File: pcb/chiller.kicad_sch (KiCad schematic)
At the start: 39 parts, among them J1 Conn_01x03, J10 Current Sense, J11 Conn_01x14, J12 Debug, J2 Conn_01x03, J3 Ext, J4 Conn_01x02, J5 Conn_01x02, J6 Conn_01x02, J7 Conn_01x02, J8 Conn_01x02, J9 CONN_01X02, K1 G5LE-1, K2 G6B-1114C-US5DC, Q1 MMBT3904, Q2 MMBT3904, Q3 BSS138, Q4 BSS138, U1 ESP32-WROOM-32, U2 DSN-MINI-360, U3 AP1117-33

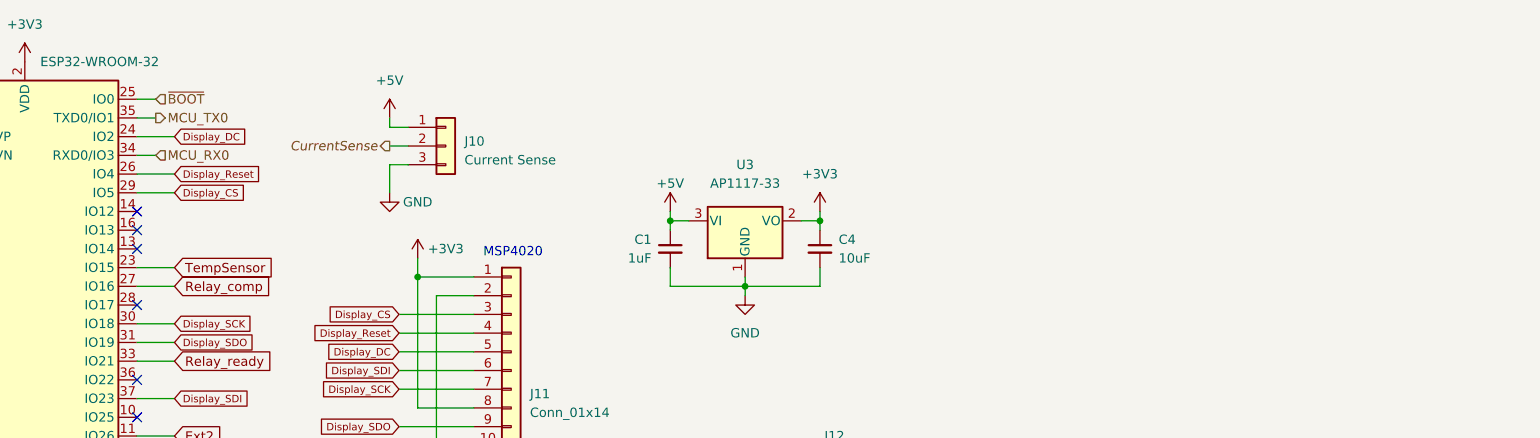
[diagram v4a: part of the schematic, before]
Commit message: Finish routing.
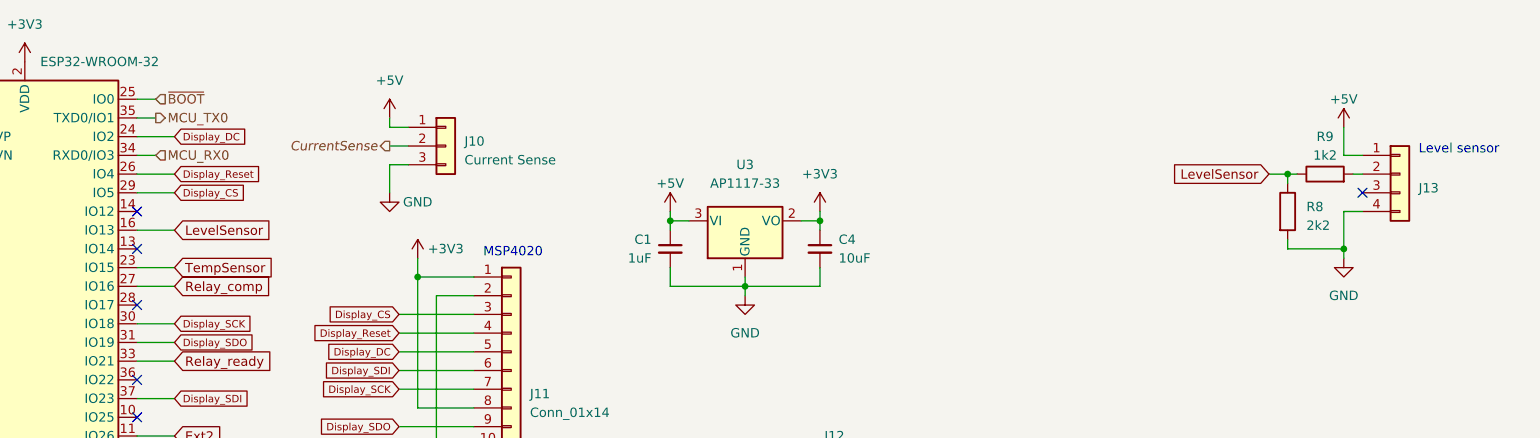
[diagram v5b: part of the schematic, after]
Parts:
- added J13: Conn_01x04, Connector_JST:JST_XH_B4B-XH-A_1x04_P2.50mm_Vertical, symbol Connector_Generic:Conn_01x04
- added R8: 2k2, Resistor_SMD:R_0603_1608Metric, symbol Device:R
- added R9: 1k2, Resistor_SMD:R_0603_1608Metric, symbol Device:R
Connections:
- net +5V: now also J13.1 (Pin_1)
- net GND: now also J13.4 (Pin_4), R8.2
- net LevelSensor: now reaches U1.16 (IO13)
- net LevelSensor: now also R8.1, R9.1
- new net: J13.2 (Pin_2), R9.2
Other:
- note added: "Level sensor"
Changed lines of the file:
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@@
   (junction (at 176.53 203.2) (diameter 1.016) (color 0 0 0 0)
   )
+  (junction (at 245.11 39.37) (diameter 0) (color 0 0 0 0)
+  )
   (junction (at 121.92 175.26) (diameter 0) (color 0 0 0 0)
   )
@@
   )
   (junction (at 163.83 175.26) (diameter 0) (color 0 0 0 0)
+  )
+  (junction (at 252.73 49.53) (diameter 0) (color 0 0 0 0)
   )
   (junction (at 163.83 149.86) (diameter 0) (color 0 0 0 0)
@@
   (no_connect (at 138.43 132.08))
   (no_connect (at 88.9 67.31))
-  (no_connect (at 88.9 46.99))
   (no_connect (at 134.62 76.2))
   (no_connect (at 134.62 81.28))
@@
   (no_connect (at 88.9 57.15))
   (no_connect (at 88.9 80.01))
+  (no_connect (at 255.27 41.91))
   (no_connect (at 134.62 86.36))
   (no_connect (at 88.9 44.45))
@@
     (stroke (width 0) (type default))
   )
+  (wire (pts (xy 254 39.37) (xy 255.27 39.37))
+    (stroke (width 0) (type default))
+  )
   (wire (pts (xy 35.56 83.82) (xy 35.56 85.09))
     (stroke (width 0) (type default))
@@
     (stroke (width 0) (type default))
   )
+  (wire (pts (xy 245.11 39.37) (xy 245.11 40.64))
+    (stroke (width 0) (type default))
+  )
   (wire (pts (xy 88.9 39.37) (xy 93.98 39.37))
     (stroke (width 0) (type default))
@@
   )
   (wire (pts (xy 124.46 60.96) (xy 134.62 60.96))
+    (stroke (width 0) (type default))
+  )
+  (wire (pts (xy 252.73 44.45) (xy 255.27 44.45))
     (stroke (width 0) (type default))
   )
@@
     (stroke (width 0) (type solid))
   )
+  (wire (pts (xy 252.73 49.53) (xy 252.73 50.8))
+    (stroke (width 0) (type default))
+  )
+  (wire (pts (xy 252.73 36.83) (xy 255.27 36.83))
+    (stroke (width 0) (type default))
+  )
   (wire (pts (xy 125.73 215.9) (xy 125.73 223.52))
     (stroke (width 0) (type solid))
@@
     (stroke (width 0) (type default))
   )
+  (wire (pts (xy 88.9 46.99) (xy 93.98 46.99))
+    (stroke (width 0) (type default))
+  )
   (wire (pts (xy 57.15 137.16) (xy 64.77 137.16))
     (stroke (width 0) (type default))
   )
   (wire (pts (xy 181.61 44.45) (xy 181.61 45.72))
+    (stroke (width 0) (type default))
+  )
+  (wire (pts (xy 242.57 39.37) (xy 245.11 39.37))
     (stroke (width 0) (type default))
   )
@@
     (stroke (width 0) (type default))
   )
+  (wire (pts (xy 245.11 48.26) (xy 245.11 49.53))
+    (stroke (width 0) (type default))
+  )
   (wire (pts (xy 33.02 83.82) (xy 35.56 86.36))
     (stroke (width 0) (type default))
@@
     (stroke (width 0) (type default))
   )
+  (wire (pts (xy 252.73 44.45) (xy 252.73 49.53))
+    (stroke (width 0) (type default))
+  )
+  (wire (pts (xy 245.11 49.53) (xy 252.73 49.53))
+    (stroke (width 0) (type default))
+  )
   (wire (pts (xy 24.13 78.74) (xy 27.94 78.74))
     (stroke (width 0) (type default))
@@
   )
   (wire (pts (xy 63.5 121.92) (xy 64.77 121.92))
+    (stroke (width 0) (type default))
+  )
+  (wire (pts (xy 252.73 33.02) (xy 252.73 36.83))
     (stroke (width 0) (type default))
   )
@@
   )
   (wire (pts (xy 33.02 87.63) (xy 24.13 87.63))
+    (stroke (width 0) (type default))
+  )
+  (wire (pts (xy 245.11 39.37) (xy 246.38 39.37))
     (stroke (width 0) (type default))
   )
@@
   (text "Temp sensor 2" (exclude_from_sim no)
  (at 81.28 135.89 0)
+    (effects (font (size 1.27 1.27)) (justify left bottom))
+  )
+  (text "Level sensor" (exclude_from_sim no)
+ (at 262.89 36.83 0)
     (effects (font (size 1.27 1.27)) (justify left bottom))
   )
@@
     )
   )
+  (global_label "LevelSensor" (shape input) (at 93.98 46.99 0) (fields_autoplaced)
+    (effects (font (size 1.27 1.27)) (justify left))
+    (property "Intersheetrefs" "${INTERSHEET_REFS}" (at 108.1343 46.99 0)
+      (effects (font (size 1.27 1.27)) (justify left) hide)
+    )
+  )
   (global_label "Display_Reset" (shape input) (at 124.46 60.96 180) (fields_autoplaced)
     (effects (font (size 1 1)) (justify right))
@@
     (property "Intersheetrefs" "${INTERSHEET_REFS}" (at 114.4648 58.3575 0)
       (effects (font (size 1 1)) (justify right) hide)
+    )
+  )
+  (global_label "LevelSensor" (shape input) (at 242.57 39.37 180) (fields_autoplaced)
+    (effects (font (size 1.27 1.27)) (justify right))
+    (property "Intersheetrefs" "${INTERSHEET_REFS}" (at 228.4157 39.37 0)
+      (effects (font (size 1.27 1.27)) (justify right) hide)
     )
   )
@@
     )
   )
+  (symbol (lib_id "power:GND") (at 252.73 50.8 0) (unit 1)
+    (in_bom yes) (on_board yes) (dnp no) (fields_autoplaced)
+    (property "Reference" "#PWR028" (at 252.73 57.15 0)
+      (effects (font (size 1.27 1.27)) hide)
+    )
+    (property "Value" "GND" (at 252.73 55.88 0)
+      (effects (font (size 1.27 1.27)))
+    )
+    (property "Footprint" "" (at 252.73 50.8 0)
+      (effects (font (size 1.27 1.27)) hide)
+    )
+    (property "Datasheet" "" (at 252.73 50.8 0)
+      (effects (font (size 1.27 1.27)) hide)
+    )
+    (pin "1")
+    (instances
+      (project "chiller"
+        (path "/212a0d71-cc7b-49f8-b4ca-a935e5355dca"
+          (reference "#PWR028") (unit 1)
+        )
+      )
+    )
+  )
   (symbol (lib_id "Device:R") (at 173.99 168.91 0) (unit 1)
     (in_bom yes) (on_board yes) (dnp no) (fields_autoplaced)
@@
         (path "/212a0d71-cc7b-49f8-b4ca-a935e5355dca"
           (reference "J12") (unit 1)
+        )
+      )
+    )
+  )
+  (symbol (lib_id "Connector_Generic:Conn_01x04") (at 260.35 39.37 0) (unit 1)
+    (in_bom yes) (on_board yes) (dnp no) (fields_autoplaced)
+    (property "Reference" "J13" (at 262.89 41.275 0)
+      (effects (font (size 1.27 1.27)) (justify left))
+    )
+    (property "Value" "Conn_01x04" (at 262.89 42.545 0)
+      (effects (font (size 1.27 1.27)) (justify left) hide)
+    )
+    (property "Footprint" "Connector_JST:JST_XH_B4B-XH-A_1x04_P2.50mm_Vertical" (at 260.35 39.37 0)
+      (effects (font (size 1.27 1.27)) hide)
+    )
+    (property "Datasheet" "~" (at 260.35 39.37 0)
+      (effects (font (size 1.27 1.27)) hide)
+    )
+    (pin "1")
+    (pin "2")
+    (pin "3")
+    (pin "4")
+    (instances
+      (project "chiller"
+        (path "/212a0d71-cc7b-49f8-b4ca-a935e5355dca"
+          (reference "J13") (unit 1)
         )
       )
@@
     )
   )
+  (symbol (lib_id "power:+5V") (at 252.73 33.02 0) (unit 1)
+    (in_bom yes) (on_board yes) (dnp no) (fields_autoplaced)
+    (property "Reference" "#PWR027" (at 252.73 36.83 0)
+      (effects (font (size 1.27 1.27)) hide)
+    )
+    (property "Value" "+5V" (at 252.73 29.21 0)
+      (effects (font (size 1.27 1.27)))
+    )
+    (property "Footprint" "" (at 252.73 33.02 0)
+      (effects (font (size 1.27 1.27)) hide)
+    )
+    (property "Datasheet" "" (at 252.73 33.02 0)
+      (effects (font (size 1.27 1.27)) hide)
+    )
+    (pin "1")
+    (instances
+      (project "chiller"
+        (path "/212a0d71-cc7b-49f8-b4ca-a935e5355dca"
+          (reference "#PWR027") (unit 1)
+        )
+      )
+    )
+  )
+  (symbol (lib_id "Device:R") (at 250.19 39.37 90) (unit 1)
+    (in_bom yes) (on_board yes) (dnp no) (fields_autoplaced)
+    (property "Reference" "R9" (at 250.19 34.29 90)
+      (effects (font (size 1.27 1.27)))
+    )
+    (property "Value" "1k2" (at 250.19 36.83 90)
+      (effects (font (size 1.27 1.27)))
+    )
+    (property "Footprint" "Resistor_SMD:R_0603_1608Metric" (at 250.19 41.148 90)
+      (effects (font (size 1.27 1.27)) hide)
+    )
+    (property "Datasheet" "~" (at 250.19 39.37 0)
+      (effects (font (size 1.27 1.27)) hide)
+    )
+    (pin "1")
+    (pin "2")
+    (instances
+      (project "chiller"
+        (path "/212a0d71-cc7b-49f8-b4ca-a935e5355dca"
+          (reference "R9") (unit 1)
+        )
+      )
+    )
+  )
   (symbol (lib_id "Device:R_Small") (at 165.1 92.71 0) (mirror y) (unit 1)
     (in_bom yes) (on_board yes) (dnp no)
@@
         )
       )
+    )
+  )
+  (symbol (lib_id "Device:R") (at 245.11 44.45 0) (unit 1)
+    (in_bom yes) (on_board yes) (dnp no) (fields_autoplaced)
+    (property "Reference" "R8" (at 247.65 43.815 0)
+      (effects (font (size 1.27 1.27)) (justify left))
+    )
+    (property "Value" "2k2" (at 247.65 46.355 0)
+      (effects (font (size 1.27 1.27)) (justify left))
+    )
+    (property "Footprint" "Resistor_SMD:R_0603_1608Metric" (at 243.332 44.45 90)
+      (effects (font (size 1.27 1.27)) hide)
+    )
+    (property "Datasheet" "~" (at 245.11 44.45 0)
+      (effects (font (size 1.27 1.27)) hide)
+    )
+    (pin "1")
+    (pin "2")
+    (instances
+      (project "chiller"
+        (path "/212a0d71-cc7b-49f8-b4ca-a935e5355dca"
+          (reference "R8") (unit 1)
+        )
+      )

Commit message: Cleanup.
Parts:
- C1: value 1uF -> 1u
- C4: value 10uF -> 10u
- C5: value C -> 100n
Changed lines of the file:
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@@
   (symbol (lib_id "Device:C_Small") (at 181.61 49.53 0) (unit 1)
     (in_bom yes) (on_board yes) (dnp no) (fields_autoplaced)
-    (property "Reference" "C4" (at 184.15 48.2599 0)
-      (effects (font (size 1.27 1.27)) (justify left))
-    )
-    (property "Value" "10uF" (at 184.15 50.7999 0)
+    (property "Reference" "C4" (at 184.15 48.9013 0)
+      (effects (font (size 1.27 1.27)) (justify left))
+    )
+    (property "Value" "10u" (at 184.15 51.4413 0)
       (effects (font (size 1.27 1.27)) (justify left))
     )
@@
       (effects (font (size 1.27 1.27)) (justify left))
     )
-    (property "Value" "C" (at 36.83 41.275 0)
+    (property "Value" "100n" (at 36.83 41.275 0)
       (effects (font (size 1.27 1.27)) (justify left))
     )
@@
       (effects (font (size 1.27 1.27)) (justify left))
     )
-    (property "Value" "1uF" (at 158.75 50.7999 0)
-      (effects (font (size 1.27 1.27)) (justify left))
-    )
+    (property "Value" "1u" (at 158.75 50.7999 0)
+      (effects (font (size 1.27 1.27)) (justify left))
+    )

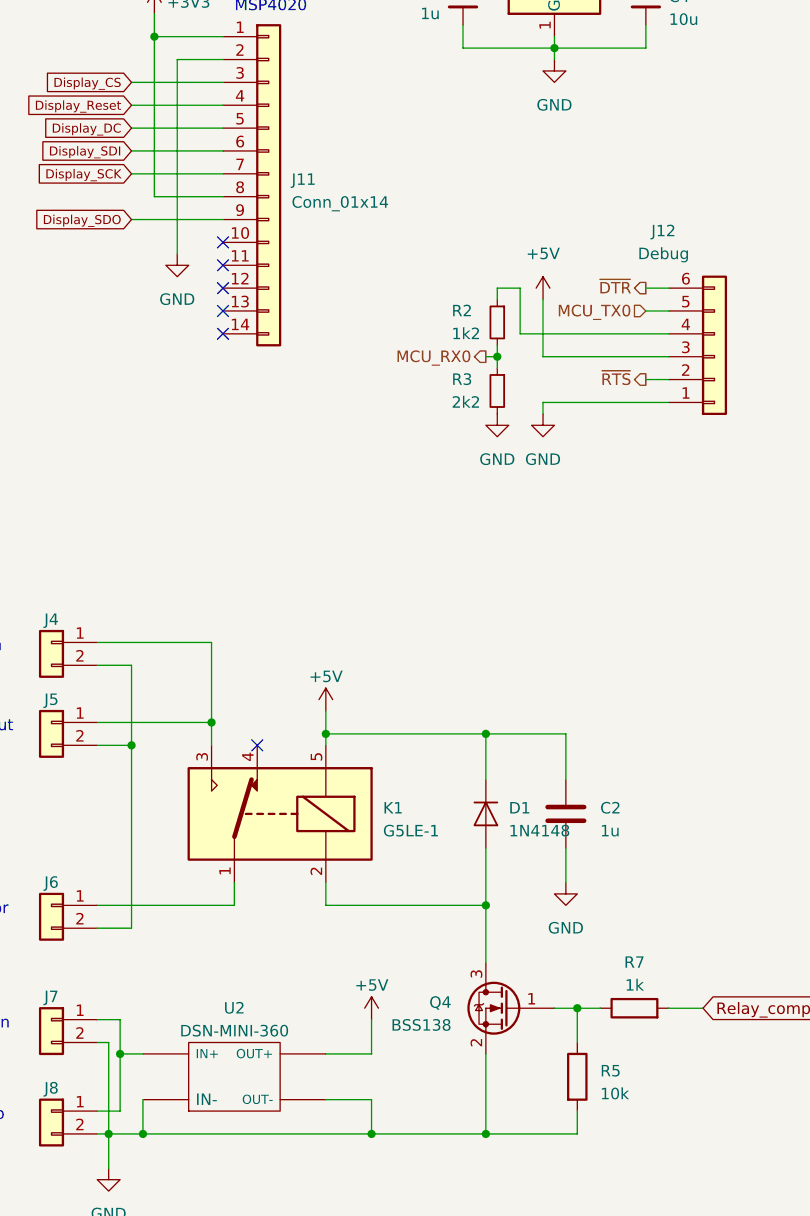
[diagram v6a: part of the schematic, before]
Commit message: Add diodes.
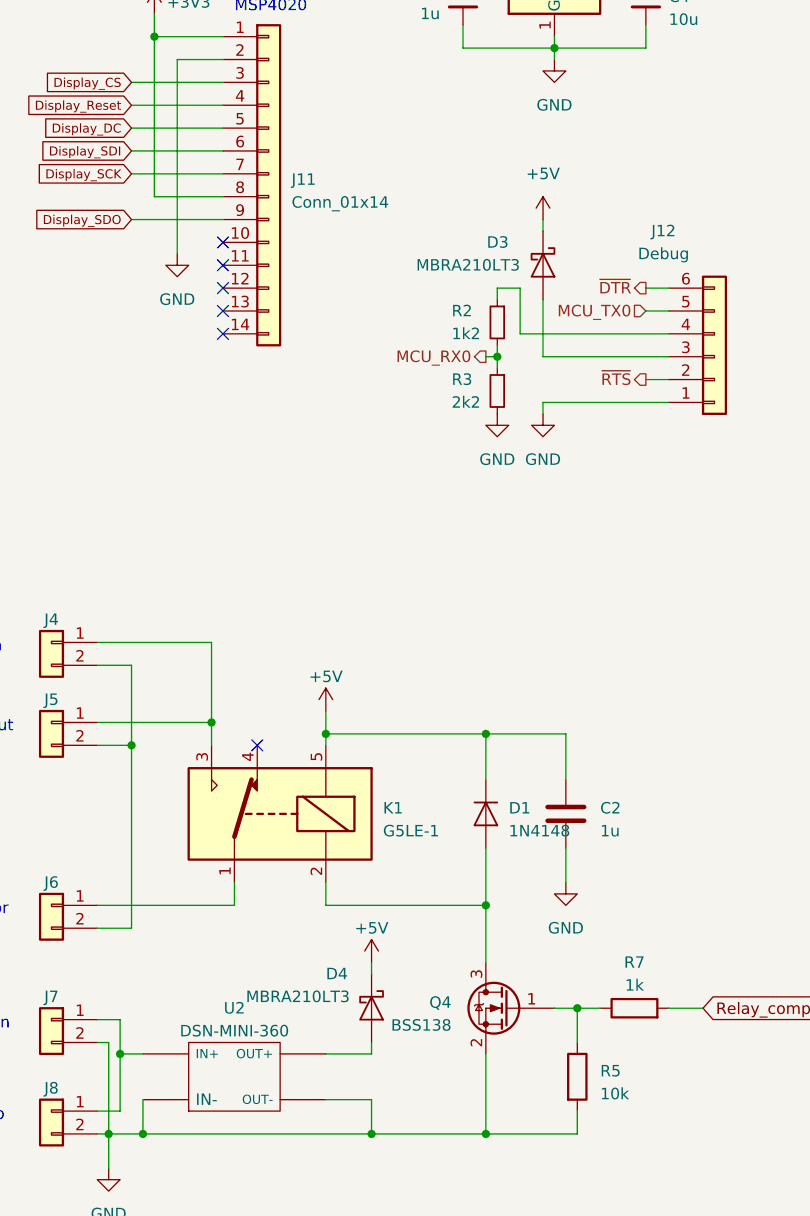
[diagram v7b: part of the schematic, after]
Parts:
- added D3, D4: MBRA210LT3, Diode_SMD:D_SMA, symbol Device:D_Schottky
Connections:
- net +5V: now also D3.1 (K), D4.1 (K); no longer J12.3 (Pin_3), U2.OUT+
- new net: D3.2 (A), J12.3 (Pin_3)
- new net: D4.2 (A), U2.OUT+
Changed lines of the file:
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@@
+    (stroke (width 0) (type default))
+  )
+  (wire (pts (xy 151.13 165.1) (xy 151.13 166.37))
     (stroke (width 0) (type default))
   )
@@
     (stroke (width 0) (type default))
   )
-  (wire (pts (xy 151.13 162.56) (xy 151.13 166.37))
-    (stroke (width 0) (type default))
-  )
   (wire (pts (xy 120.65 165.1) (xy 121.92 165.1))
     (stroke (width 0) (type default))
@@
     (stroke (width 0) (type default))
   )
+  (wire (pts (xy 170.18 73.66) (xy 170.18 74.93))
+    (stroke (width 0) (type default))
+  )
   (wire (pts (xy 165.1 87.63) (xy 165.1 88.9))
     (stroke (width 0) (type default))
@@
   )
   (wire (pts (xy 242.57 39.37) (xy 245.11 39.37))
+    (stroke (width 0) (type default))
+  )
+  (wire (pts (xy 151.13 156.21) (xy 151.13 157.48))
     (stroke (width 0) (type default))
   )
@@
     )
   )
-  (symbol (lib_id "power:+5V") (at 151.13 162.56 0) (unit 1)
-    (in_bom yes) (on_board yes) (dnp no) (fields_autoplaced)
-    (property "Reference" "#PWR014" (at 151.13 166.37 0)
-      (effects (font (size 1.27 1.27)) hide)
-    )
-    (property "Value" "+5V" (at 151.13 158.75 0)
-      (effects (font (size 1.27 1.27)))
-    )
-    (property "Footprint" "" (at 151.13 162.56 0)
-      (effects (font (size 1.27 1.27)) hide)
-    )
-    (property "Datasheet" "" (at 151.13 162.56 0)
+  (symbol (lib_id "Device:D_Schottky") (at 170.18 78.74 270) (unit 1)
+    (in_bom yes) (on_board yes) (dnp no)
+    (property "Reference" "D3" (at 166.37 76.2 90)
+      (effects (font (size 1.27 1.27)) (justify right))
+    )
+    (property "Value" "MBRA210LT3 " (at 167.64 78.74 90)
+      (effects (font (size 1.27 1.27)) (justify right))
+    )
+    (property "Footprint" "Diode_SMD:D_SMA" (at 170.18 78.74 0)
+      (effects (font (size 1.27 1.27)) hide)
+    )
+    (property "Datasheet" "~" (at 170.18 78.74 0)
+      (effects (font (size 1.27 1.27)) hide)
+    )
+    (pin "1")
+    (pin "2")
+    (instances
+      (project "chiller"
+        (path "/212a0d71-cc7b-49f8-b4ca-a935e5355dca"
+          (reference "D3") (unit 1)
+        )
+      )
+    )
+  )
+  (symbol (lib_id "power:+5V") (at 151.13 156.21 0) (unit 1)
+    (in_bom yes) (on_board yes) (dnp no) (fields_autoplaced)
+    (property "Reference" "#PWR014" (at 151.13 160.02 0)
+      (effects (font (size 1.27 1.27)) hide)
+    )
+    (property "Value" "+5V" (at 151.13 152.4 0)
+      (effects (font (size 1.27 1.27)))
+    )
+    (property "Footprint" "" (at 151.13 156.21 0)
+      (effects (font (size 1.27 1.27)) hide)
+    )
+    (property "Datasheet" "" (at 151.13 156.21 0)
       (effects (font (size 1.27 1.27)) hide)
     )
@@
     )
   )
-  (symbol (lib_id "power:+5V") (at 170.18 82.55 0) (unit 1)
-    (in_bom yes) (on_board yes) (dnp no) (fields_autoplaced)
-    (property "Reference" "#PWR018" (at 170.18 86.36 0)
-      (effects (font (size 1.27 1.27)) hide)
-    )
-    (property "Value" "+5V" (at 170.18 77.47 0)
-      (effects (font (size 1.27 1.27)))
-    )
-    (property "Footprint" "" (at 170.18 82.55 0)
-      (effects (font (size 1.27 1.27)) hide)
-    )
-    (property "Datasheet" "" (at 170.18 82.55 0)
+  (symbol (lib_id "power:+5V") (at 170.18 73.66 0) (unit 1)
+    (in_bom yes) (on_board yes) (dnp no) (fields_autoplaced)
+    (property "Reference" "#PWR018" (at 170.18 77.47 0)
+      (effects (font (size 1.27 1.27)) hide)
+    )
+    (property "Value" "+5V" (at 170.18 68.58 0)
+      (effects (font (size 1.27 1.27)))
+    )
+    (property "Footprint" "" (at 170.18 73.66 0)
+      (effects (font (size 1.27 1.27)) hide)
+    )
+    (property "Datasheet" "" (at 170.18 73.66 0)
       (effects (font (size 1.27 1.27)) hide)
     )
@@
         )
       )
+    )
+  )
+  (symbol (lib_id "Device:D_Schottky") (at 151.13 161.29 270) (unit 1)
+    (in_bom yes) (on_board yes) (dnp no)
+    (property "Reference" "D4" (at 146.05 157.48 90)
+      (effects (font (size 1.27 1.27)) (justify left))
+    )
+    (property "Value" "MBRA210LT3 " (at 137.16 160.02 90)
+      (effects (font (size 1.27 1.27)) (justify left))
+    )
+    (property "Footprint" "Diode_SMD:D_SMA" (at 151.13 161.29 0)
+      (effects (font (size 1.27 1.27)) hide)
+    )
+    (property "Datasheet" "~" (at 151.13 161.29 0)
+      (effects (font (size 1.27 1.27)) hide)
+    )
+    (pin "1")
+    (pin "2")
+    (instances
+      (project "chiller"
+        (path "/212a0d71-cc7b-49f8-b4ca-a935e5355dca"
+          (reference "D4") (unit 1)
+        )
+      )

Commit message: Start adding forgotten features.
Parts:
- added J14: Flow sensor, Connector_JST:JST_XH_B3B-XH-A_1x03_P2.50mm_Vertical, symbol Connector_Generic:Conn_01x03
- added J15: Fan, Connector_JST:JST_XH_B2B-XH-A_1x02_P2.50mm_Vertical, symbol Connector_Generic:Conn_01x02
- added Q5: BSS138, Package_TO_SOT_SMD:SOT-23, symbol Device:Q_NMOS_GSD
- added R10: 1k2, Resistor_SMD:R_0603_1608Metric, symbol Device:R
- added R11: 2k2, Resistor_SMD:R_0603_1608Metric, symbol Device:R
- J11: value Conn_01x14 -> Display; footprint Connector_PinSocket_2.54mm:PinSocket_1x14_P2.54mm_Vertical -> Connector_PinSocket_2.54mm:PinSocket_1x09_P2.54mm_Vertical; symbol Connector_Generic:Conn_01x14 -> Connector_Generic:Conn_01x09
- U1: footprint RF_Module:ESP32-WROOM-32 -> RF_Module:ESP32-WROOM-32U
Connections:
- net +5V: now also J14.1 (Pin_1)
- net GND: now also J14.3 (Pin_3), R11.2
- new net: J14.2 (Pin_2), R10.2
- new net Flow: R10.1, R11.1
- no-connect marks 23 -> 18
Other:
- note added: "FAN"
